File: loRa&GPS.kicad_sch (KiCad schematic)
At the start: 22 parts, among them J4 Conn_Coaxial, U10 RAK3172, U9 TESEO-LIV4F

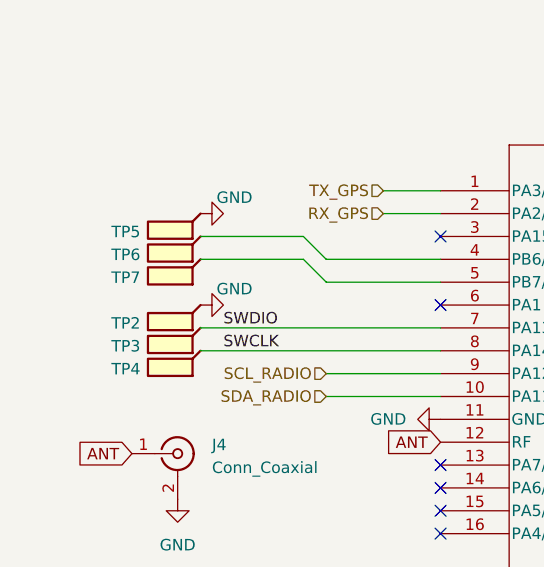
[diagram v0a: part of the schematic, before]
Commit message: fpc connector inizio
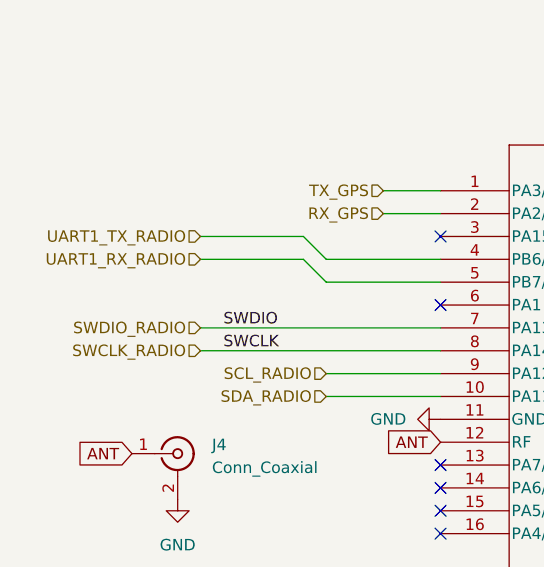
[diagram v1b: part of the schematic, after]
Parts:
- removed TP2, TP3, TP4, TP5, TP6, TP7: TestPoint_Flag, TestPoint:TestPoint_Pad_2.0x2.0mm, symbol Connector:TestPoint_Flag
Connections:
- net UART1_TX_RADIO: now reaches U10.4 (PB6/UART1_TX)
- net UART1_RX_RADIO: now reaches U10.5 (PB7/UART1_RX)
- net SWCLK renamed SWCLK_RADIO
- net SWDIO renamed SWDIO_RADIO

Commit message: aiuto
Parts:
- ANT1, BT1, C37, C39, C40, D10, D11, D8, D9, J4, JP1, R39, RN1, TP1, U10, U9: now not fitted
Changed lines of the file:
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@@
 		(exclude_from_sim no)
 		(in_bom yes)
-		(on_board yes)
-		(dnp no)
+		(on_board no)
+		(dnp yes)
 		(fields_autoplaced yes)
 		(property "Reference" "TP1"
@@
 		(exclude_from_sim no)
 		(in_bom yes)
-		(on_board yes)
-		(dnp no)
+		(on_board no)
+		(dnp yes)
 		(fields_autoplaced yes)
 		(property "Reference" "#PWR066"
@@
 		(exclude_from_sim no)
 		(in_bom yes)
-		(on_board yes)
-		(dnp no)
+		(on_board no)
+		(dnp yes)
 		(fields_autoplaced yes)
 		(property "Reference" "#PWR0122"
@@
 		(exclude_from_sim no)
 		(in_bom yes)
-		(on_board yes)
-		(dnp no)
+		(on_board no)
+		(dnp yes)
 		(fields_autoplaced yes)
 		(property "Reference" "U10"
@@
 		(exclude_from_sim no)
 		(in_bom yes)
-		(on_board yes)
-		(dnp no)
+		(on_board no)
+		(dnp yes)
 		(fields_autoplaced yes)
 		(property "Reference" "#PWR0104"
@@
 		(exclude_from_sim no)
 		(in_bom yes)
-		(on_board yes)
-		(dnp no)
+		(on_board no)
+		(dnp yes)
 		(fields_autoplaced yes)
 		(property "Reference" "J4"
@@
 		(exclude_from_sim no)
 		(in_bom yes)
-		(on_board yes)
-		(dnp no)
+		(on_board no)
+		(dnp yes)
 		(fields_autoplaced yes)
 		(property "Reference" "R39"
@@
 		(exclude_from_sim no)
 		(in_bom yes)
-		(on_board yes)
-		(dnp no)
+		(on_board no)
+		(dnp yes)
 		(fields_autoplaced yes)
 		(property "Reference" "#PWR0120"
@@
 		(exclude_from_sim no)
 		(in_bom yes)
-		(on_board yes)
-		(dnp no)
+		(on_board no)
+		(dnp yes)
 		(fields_autoplaced yes)
 		(property "Reference" "#PWR0124"
@@
 		(exclude_from_sim no)
 		(in_bom yes)
-		(on_board yes)
-		(dnp no)
+		(on_board no)
+		(dnp yes)
 		(property "Reference" "BT1"
 			(at 167.132 58.928 0)
@@
 		(exclude_from_sim no)
 		(in_bom yes)
-		(on_board yes)
-		(dnp no)
+		(on_board no)
+		(dnp yes)
 		(fields_autoplaced yes)
 		(property "Reference" "D8"
@@
 		(exclude_from_sim no)
 		(in_bom yes)
-		(on_board yes)
-		(dnp no)
+		(on_board no)
+		(dnp yes)
 		(fields_autoplaced yes)
 		(property "Reference" "RN1"
@@
 		(exclude_from_sim no)
 		(in_bom yes)
-		(on_board yes)
-		(dnp no)
+		(on_board no)
+		(dnp yes)
 		(fields_autoplaced yes)
 		(property "Reference" "ANT1"
@@
 		(exclude_from_sim no)
 		(in_bom yes)
-		(on_board yes)
-		(dnp no)
+		(on_board no)
+		(dnp yes)
 		(fields_autoplaced yes)
 		(property "Reference" "#PWR0112"
@@
 		(exclude_from_sim no)
 		(in_bom yes)
-		(on_board yes)
-		(dnp no)
+		(on_board no)
+		(dnp yes)
 		(property "Reference" "D11"
 			(at 159.258 127.254 0)
@@
 		(exclude_from_sim no)
 		(in_bom yes)
-		(on_board yes)
-		(dnp no)
+		(on_board no)
+		(dnp yes)
 		(fields_autoplaced yes)
 		(property "Reference" "#PWR0126"
@@
 		(exclude_from_sim no)
 		(in_bom yes)
-		(on_board yes)
-		(dnp no)
+		(on_board no)
+		(dnp yes)
 		(property "Reference" "C37"
 			(at 149.098 59.436 0)
@@
 		(exclude_from_sim no)
 		(in_bom yes)
-		(on_board yes)
-		(dnp no)
+		(on_board no)
+		(dnp yes)
 		(property "Reference" "D10"
 			(at 171.196 117.602 0)
@@
 		(exclude_from_sim no)
 		(in_bom yes)
-		(on_board yes)
-		(dnp no)
+		(on_board no)
+		(dnp yes)
 		(fields_autoplaced yes)
 		(property "Reference" "#PWR068"
@@
 		(exclude_from_sim no)
 		(in_bom yes)
-		(on_board yes)
-		(dnp no)
+		(on_board no)
+		(dnp yes)
 		(fields_autoplaced yes)
 		(property "Reference" "#PWR0123"
@@
 		(exclude_from_sim no)
 		(in_bom no)
-		(on_board yes)
-		(dnp no)
+		(on_board no)
+		(dnp yes)
 		(property "Reference" "JP1"
 			(at 44.45 74.422 0)
@@
 		(exclude_from_sim no)
 		(in_bom yes)
-		(on_board yes)
-		(dnp no)
+		(on_board no)
+		(dnp yes)
 		(fields_autoplaced yes)
 		(property "Reference" "U9"
@@
 		(exclude_from_sim no)
 		(in_bom yes)
-		(on_board yes)
-		(dnp no)
+		(on_board no)
+		(dnp yes)
 		(fields_autoplaced yes)
 		(property "Reference" "#PWR087"
@@
 		(exclude_from_sim no)
 		(in_bom yes)
-		(on_board yes)
-		(dnp no)
+		(on_board no)
+		(dnp yes)
 		(fields_autoplaced yes)
 		(property "Reference" "C40"
@@
 		(exclude_from_sim no)
 		(in_bom yes)
-		(on_board yes)
-		(dnp no)
+		(on_board no)
+		(dnp yes)
 		(fields_autoplaced yes)
 		(property "Reference" "#PWR0121"
@@
 		(exclude_from_sim no)
 		(in_bom yes)
-		(on_board yes)
-		(dnp no)
+		(on_board no)
+		(dnp yes)
 		(fields_autoplaced yes)
 		(property "Reference" "#PWR0113"
@@
 		(exclude_from_sim no)
 		(in_bom yes)
-		(on_board yes)
-		(dnp no)
+		(on_board no)
+		(dnp yes)
 		(property "Reference" "D9"
 			(at 156.464 110.236 0)
@@
 		(exclude_from_sim no)
 		(in_bom yes)
-		(on_board yes)
-		(dnp no)
+		(on_board no)
+		(dnp yes)
 		(fields_autoplaced yes)
 		(property "Reference" "#PWR0125"
@@
 		(exclude_from_sim no)
 		(in_bom yes)
-		(on_board yes)
-		(dnp no)
+		(on_board no)
+		(dnp yes)
 		(fields_autoplaced yes)
 		(property "Reference" "C39"
@@
 		(exclude_from_sim no)
 		(in_bom yes)
-		(on_board yes)
-		(dnp no)
+		(on_board no)
+		(dnp yes)
 		(fields_autoplaced yes)
 		(property "Reference" "#PWR088"
@@
 		(exclude_from_sim no)
 		(in_bom yes)
-		(on_board yes)
-		(dnp no)
+		(on_board no)
+		(dnp yes)
 		(fields_autoplaced yes)
 		(property "Reference" "#PWR058"
